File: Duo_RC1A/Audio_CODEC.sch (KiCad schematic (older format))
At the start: 31 parts

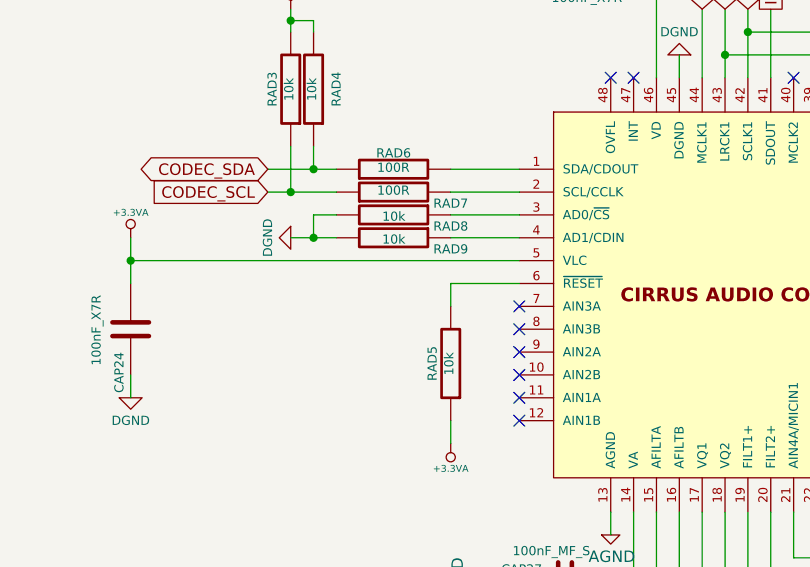
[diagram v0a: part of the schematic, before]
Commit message: Removed some of the audio CODEC signals for Minimal Viable Product. Need to change the 3.3V regulator to the Top Board.
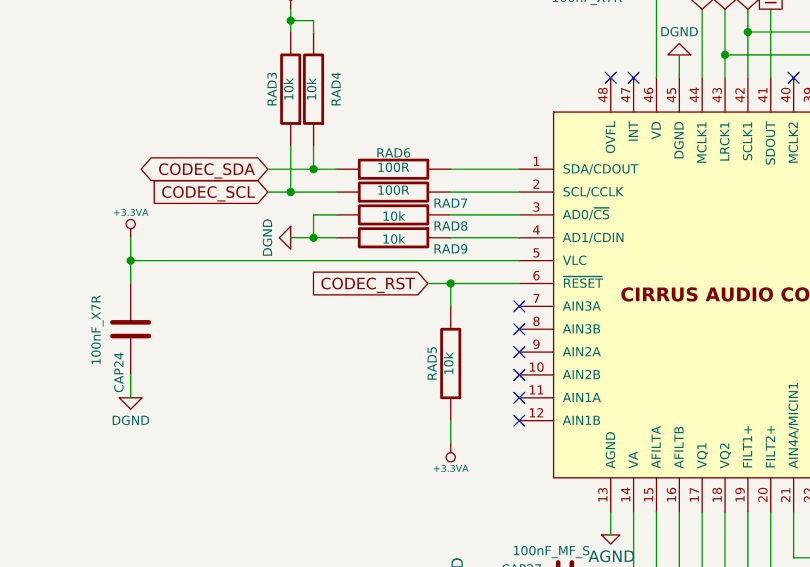
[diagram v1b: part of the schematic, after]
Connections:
- net CODEC_RST: now reaches RAD5.2, UA9.6 (~RESET)
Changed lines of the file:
@@
 Connection ~ 4000 3000
 Wire Wire Line
-	4700 3400 5000 3400
+	4600 3400 5000 3400
 Wire Wire Line
 	4000 2200 4000 2300
@@
 Wire Wire Line
 	2450 5650 2450 5550
+Text GLabel 4600 3400 0    50   Input ~ 0
+CODEC_RST
+Connection ~ 4700 3400
 $EndSCHEMATC

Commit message: Wrking on the sound. Changed the board size.
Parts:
- removed CAP29: 10uF, Duo_Audio_HMI_RC1A:SM0805, symbol CP1
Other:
- moved on the sheet: CAP24, CAP30
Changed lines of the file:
@@
 L C CAP24
 U 1 1 53695313
-P 3300 3600
-F 0 "CAP24" V 3350 3700 40  0000 L CNN
-F 1 "100nF_X7R" V 3450 3450 40  0000 L CNN
-F 2 "Duo_Audio_HMI_RC1A:SM0603" H 3338 3450 30  0001 C CNN
-F 3 "~" H 3300 3600 60  0000 C CNN
-	1    3300 3600
+P 3600 3600
+F 0 "CAP24" V 3650 3700 40  0000 L CNN
+F 1 "100nF_X7R" V 3750 3450 40  0000 L CNN
+F 2 "Duo_Audio_HMI_RC1A:SM0603" H 3638 3450 30  0001 C CNN
+F 3 "~" H 3600 3600 60  0000 C CNN
+	1    3600 3600
 	-1   0    0    1
 $EndComp
@@
 	4700 4000 4700 4100
 Wire Wire Line
-	3300 3200 3300 3400
+	3600 3200 3600 3400
 $Comp
 L +3.3VA #PWR0181
 U 1 1 53696D8F
-P 3300 3200
-F 0 "#PWR0181" H 3300 3160 30  0001 C CNN
-F 1 "+3.3VA" H 3300 3310 30  0000 C CNN
-F 2 "~" H 3300 3200 60  0000 C CNN
-F 3 "~" H 3300 3200 60  0000 C CNN
-	1    3300 3200
-	1    0    0    -1
-$EndComp
-$Comp
-L CP1 CAP29
-U 1 1 53697CB5
-P 5300 1800
-F 0 "CAP29" V 5250 1550 40  0000 L CNN
-F 1 "10uF" V 5440 1720 40  0000 L CNN
-F 2 "Duo_Audio_HMI_RC1A:SM0805" H 5300 1800 60  0001 C CNN
-F 3 "~" H 5300 1800 60  0000 C CNN
-	1    5300 1800
-	0    1    -1   0
+P 3600 3200
+F 0 "#PWR0181" H 3600 3160 30  0001 C CNN
+F 1 "+3.3VA" H 3600 3310 30  0000 C CNN
+F 2 "~" H 3600 3200 60  0000 C CNN
+F 3 "~" H 3600 3200 60  0000 C CNN
+	1    3600 3200
+	1    0    0    -1
 $EndComp
 $Comp
 L C CAP30
 U 1 1 53697CBB
-P 5300 2000
-F 0 "CAP30" V 5350 2100 40  0000 L CNN
-F 1 "100nF_X7R" V 5450 1850 40  0000 L CNN
-F 2 "Duo_Audio_HMI_RC1A:SM0603" H 5338 1850 30  0001 C CNN
-F 3 "~" H 5300 2000 60  0000 C CNN
-	1    5300 2000
+P 5300 2200
+F 0 "CAP30" V 5150 2100 40  0000 L CNN
+F 1 "100nF_X7R" V 5450 2050 40  0000 L CNN
+F 2 "Duo_Audio_HMI_RC1A:SM0603" H 5338 2050 30  0001 C CNN
+F 3 "~" H 5300 2200 60  0000 C CNN
+	1    5300 2200
 	0    -1   1    0
 $EndComp
 Wire Wire Line
-	4900 2000 5100 2000
-Wire Wire Line
-	5000 2000 5000 1800
-Wire Wire Line
-	5000 1800 5100 1800
-Connection ~ 5000 2000
+	5000 2200 5100 2200
 $Comp
 L +3.3VA #PWR0182
 U 1 1 53697CCF
-P 5600 1700
-F 0 "#PWR0182" H 5600 1660 30  0001 C CNN
-F 1 "+3.3VA" H 5600 1810 30  0000 C CNN
-F 2 "~" H 5600 1700 60  0000 C CNN
-F 3 "~" H 5600 1700 60  0000 C CNN
-	1    5600 1700
-	1    0    0    -1
-$EndComp
-Wire Wire Line
-	5600 1700 5600 2500
-Wire Wire Line
-	5600 1800 5500 1800
-Wire Wire Line
-	5500 2000 5600 2000
-Connection ~ 5600 2000
-Connection ~ 5600 1800
+P 5600 2100
+F 0 "#PWR0182" H 5600 2060 30  0001 C CNN
+F 1 "+3.3VA" H 5600 2210 30  0000 C CNN
+F 2 "~" H 5600 2100 60  0000 C CNN
+F 3 "~" H 5600 2100 60  0000 C CNN
+	1    5600 2100
+	1    0    0    -1
+$EndComp
+Wire Wire Line
+	5600 2100 5600 2500
+Wire Wire Line
+	5500 2200 5600 2200
+Connection ~ 5600 2200
 $Comp
 L DGND #PWR0183
 U 1 1 53698221
-P 4900 2000
-F 0 "#PWR0183" H 4900 2000 40  0001 C CNN
-F 1 "DGND" H 4900 1900 40  0000 C CNN
-F 2 "~" H 4900 2000 60  0000 C CNN
-F 3 "~" H 4900 2000 60  0000 C CNN
-	1    4900 2000
+P 5000 2200
+F 0 "#PWR0183" H 5000 2200 40  0001 C CNN
+F 1 "DGND" H 5000 2100 40  0000 C CNN
+F 2 "~" H 5000 2200 60  0000 C CNN
+F 3 "~" H 5000 2200 60  0000 C CNN
+	1    5000 2200
 	0    1    1    0
 $EndComp
@@
 L DGND #PWR0185
 U 1 1 5369C1E0
-P 3300 3900
-F 0 "#PWR0185" H 3300 3900 40  0001 C CNN
-F 1 "DGND" H 3300 3800 40  0000 C CNN
-F 2 "~" H 3300 3900 60  0000 C CNN
-F 3 "~" H 3300 3900 60  0000 C CNN
-	1    3300 3900
+P 3600 3900
+F 0 "#PWR0185" H 3600 3900 40  0001 C CNN
+F 1 "DGND" H 3600 3800 40  0000 C CNN
+F 2 "~" H 3600 3900 60  0000 C CNN
+F 3 "~" H 3600 3900 60  0000 C CNN
+	1    3600 3900
 	1    0    0    -1
 $EndComp
@@
 NoConn ~ 5000 3500
 Wire Wire Line
-	3300 3900 3300 3800
-Wire Wire Line
-	5000 3300 3300 3300
-Connection ~ 3300 3300
+	3600 3900 3600 3800
+Wire Wire Line
+	5000 3300 3600 3300
+Connection ~ 3600 3300
 Wire Wire Line
 	5800 2200 5800 2500

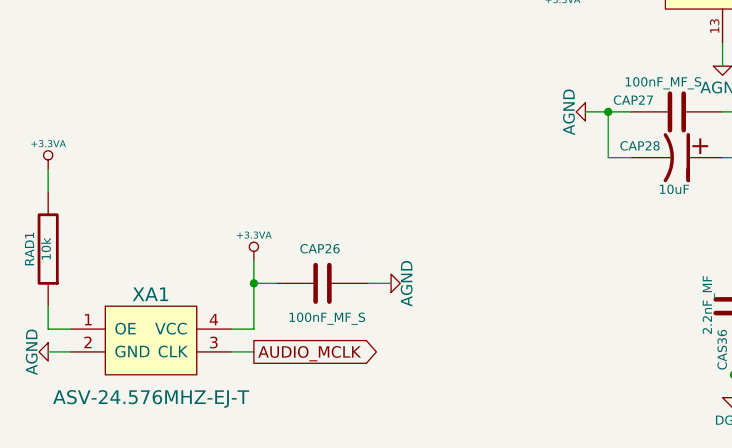
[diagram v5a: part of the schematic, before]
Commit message: USB OTG and HOST traks done.
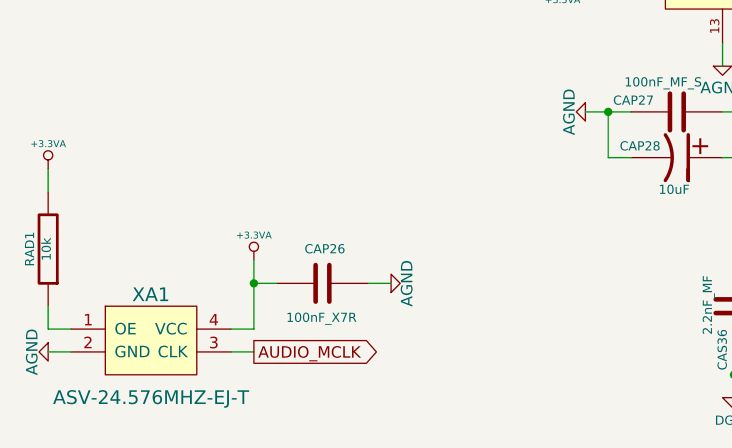
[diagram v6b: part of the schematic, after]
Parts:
- CAP26: value 100nF_MF_S -> 100nF_X7R; footprint Duo_Audio_HMI_RC1A:CapacitorMetalFilm_7.2x2.5MM_P5MM -> Duo_Audio_HMI_RC1A:SM0603
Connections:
- net +3.3VA: now also CAP26.1; no longer CAP26.2
- net AGND: now also CAP26.2; no longer CAP26.1
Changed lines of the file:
@@
 $EndComp
 $Comp
-L AGND #PWR0182
+L AGND #PWR0186
 U 1 1 5369103E
 P 2450 5750
-F 0 "#PWR0182" H 2450 5750 40  0001 C CNN
+F 0 "#PWR0186" H 2450 5750 40  0001 C CNN
 F 1 "AGND" H 2450 5680 50  0000 C CNN
 F 2 "~" H 2450 5750 60  0000 C CNN
@@
 $EndComp
 $Comp
-L +3.3VA #PWR0183
+L +3.3VA #PWR0187
 U 1 1 53691514
 P 3350 5350
-F 0 "#PWR0183" H 3350 5310 30  0001 C CNN
+F 0 "#PWR0187" H 3350 5310 30  0001 C CNN
 F 1 "+3.3VA" H 3350 5460 30  0000 C CNN
 F 2 "~" H 3350 5350 60  0000 C CNN
@@
 $EndComp
 $Comp
-L C CAP26
-U 1 1 5369152B
-P 3650 5450
-F 0 "CAP26" V 3500 5350 40  0000 L CNN
-F 1 "100nF_MF_S" V 3800 5300 40  0000 L CNN
-F 2 "Duo_Audio_HMI_RC1A:CapacitorMetalFilm_7.2x2.5MM_P5MM" H 3688 5300 30  0001 C CNN
-F 3 "~" H 3650 5450 60  0000 C CNN
-	1    3650 5450
-	0    1    1    0
-$EndComp
-$Comp
-L AGND #PWR0184
+L AGND #PWR0188
 U 1 1 53691576
 P 3950 5450
-F 0 "#PWR0184" H 3950 5450 40  0001 C CNN
+F 0 "#PWR0188" H 3950 5450 40  0001 C CNN
 F 1 "AGND" H 3950 5380 50  0000 C CNN
 F 2 "~" H 3950 5450 60  0000 C CNN
@@
 $EndComp
 $Comp
-L +3.3VA #PWR0185
+L +3.3VA #PWR0189
 U 1 1 536967F3
 P 4000 2200
-F 0 "#PWR0185" H 4000 2160 30  0001 C CNN
+F 0 "#PWR0189" H 4000 2160 30  0001 C CNN
 F 1 "+3.3VA" H 4000 2310 30  0000 C CNN
 F 2 "~" H 4000 2200 60  0000 C CNN
@@
 	3600 3200 3600 3400
 $Comp
-L +3.3VA #PWR0186
+L +3.3VA #PWR0190
 U 1 1 53696D8F
 P 3600 3200
-F 0 "#PWR0186" H 3600 3160 30  0001 C CNN
+F 0 "#PWR0190" H 3600 3160 30  0001 C CNN
 F 1 "+3.3VA" H 3600 3310 30  0000 C CNN
 F 2 "~" H 3600 3200 60  0000 C CNN
@@
 	5000 2200 5100 2200
 $Comp
-L +3.3VA #PWR0187
+L +3.3VA #PWR0191
 U 1 1 53697CCF
 P 5600 2100
-F 0 "#PWR0187" H 5600 2060 30  0001 C CNN
+F 0 "#PWR0191" H 5600 2060 30  0001 C CNN
 F 1 "+3.3VA" H 5600 2210 30  0000 C CNN
 F 2 "~" H 5600 2100 60  0000 C CNN
@@
 Connection ~ 5600 2200
 $Comp
-L DGND #PWR0188
+L DGND #PWR0192
 U 1 1 53698221
 P 5000 2200
-F 0 "#PWR0188" H 5000 2200 40  0001 C CNN
+F 0 "#PWR0192" H 5000 2200 40  0001 C CNN
 F 1 "DGND" H 5000 2100 40  0000 C CNN
 F 2 "~" H 5000 2200 60  0000 C CNN
@@
 $EndComp
 $Comp
-L DGND #PWR0189
+L DGND #PWR0193
 U 1 1 53698262
 P 5700 2400
-F 0 "#PWR0189" H 5700 2400 40  0001 C CNN
+F 0 "#PWR0193" H 5700 2400 40  0001 C CNN
 F 1 "DGND" H 5700 2300 40  0000 C CNN
 F 2 "~" H 5700 2400 60  0000 C CNN
@@
 Connection ~ 5900 2400
 $Comp
-L DGND #PWR0190
+L DGND #PWR0194
 U 1 1 5369C1E0
 P 3600 3900
-F 0 "#PWR0190" H 3600 3900 40  0001 C CNN
+F 0 "#PWR0194" H 3600 3900 40  0001 C CNN
 F 1 "DGND" H 3600 3800 40  0000 C CNN
 F 2 "~" H 3600 3900 60  0000 C CNN
@@
 $EndComp
 $Comp
-L AGND #PWR0191
+L AGND #PWR0195
 U 1 1 5369C69C
 P 5400 4500
-F 0 "#PWR0191" H 5400 4500 40  0001 C CNN
+F 0 "#PWR0195" H 5400 4500 40  0001 C CNN
 F 1 "AGND" H 5405 4405 50  0000 C CNN
 F 2 "~" H 5400 4500 60  0000 C CNN
@@
 	5400 4400 5400 4500
 $Comp
-L AGND #PWR0192
+L AGND #PWR0196
 U 1 1 5369C6F4
 P 7000 3400
-F 0 "#PWR0192" H 7000 3400 40  0001 C CNN
+F 0 "#PWR0196" H 7000 3400 40  0001 C CNN
 F 1 "AGND" H 7000 3330 50  0000 C CNN
 F 2 "~" H 7000 3400 60  0000 C CNN
@@
 	7500 2700 7600 2700
 $Comp
-L +3.3VA #PWR0193
+L +3.3VA #PWR0197
 U 1 1 5369D63F
 P 7000 2600
-F 0 "#PWR0193" H 7000 2560 30  0001 C CNN
+F 0 "#PWR0197" H 7000 2560 30  0001 C CNN
 F 1 "+3.3VA" H 7000 2710 30  0000 C CNN
 F 2 "~" H 7000 2600 60  0000 C CNN
@@
 Connection ~ 7000 2700
 $Comp
-L DGND #PWR0194
+L DGND #PWR0198
 U 1 1 5369D64A
 P 7600 2700
-F 0 "#PWR0194" H 7600 2700 40  0001 C CNN
+F 0 "#PWR0198" H 7600 2700 40  0001 C CNN
 F 1 "DGND" H 7600 2600 40  0000 C CNN
 F 2 "~" H 7600 2700 60  0000 C CNN
@@
 Connection ~ 5500 4900
 $Comp
-L +5VA #PWR0195
+L +5VA #PWR0199
 U 1 1 5369E57F
 P 5500 5000
-F 0 "#PWR0195" H 5500 5130 20  0001 C CNN
+F 0 "#PWR0199" H 5500 5130 20  0001 C CNN
 F 1 "+5VA" H 5500 5100 30  0000 C CNN
 F 2 "~" H 5500 5000 60  0000 C CNN
@@
 Connection ~ 6150 5850
 $Comp
-L DGND #PWR0196
+L DGND #PWR0200
 U 1 1 536A0C40
 P 6150 5950
-F 0 "#PWR0196" H 6150 5950 40  0001 C CNN
+F 0 "#PWR0200" H 6150 5950 40  0001 C CNN
 F 1 "DGND" H 6150 5850 40  0000 C CNN
 F 2 "~" H 6150 5950 60  0000 C CNN
@@
 $EndComp
 $Comp
-L AGND #PWR0197
+L AGND #PWR0201
 U 1 1 536A0C51
 P 4800 4700
-F 0 "#PWR0197" H 4800 4700 40  0001 C CNN
+F 0 "#PWR0201" H 4800 4700 40  0001 C CNN
 F 1 "AGND" H 4800 4630 50  0000 C CNN
 F 2 "~" H 4800 4700 60  0000 C CNN
@@
 $EndComp
 $Comp
-L DGND #PWR0198
+L DGND #PWR0202
 U 1 1 536A11E5
 P 5450 5950
-F 0 "#PWR0198" H 5450 5950 40  0001 C CNN
+F 0 "#PWR0202" H 5450 5950 40  0001 C CNN
 F 1 "DGND" H 5450 5850 40  0000 C CNN
 F 2 "~" H 5450 5950 60  0000 C CNN
@@
 Connection ~ 6700 5850
 $Comp
-L DGND #PWR0199
+L DGND #PWR0203
 U 1 1 536A12DC
 P 6700 5950
-F 0 "#PWR0199" H 6700 5950 40  0001 C CNN
+F 0 "#PWR0203" H 6700 5950 40  0001 C CNN
 F 1 "DGND" H 6700 5850 40  0000 C CNN
 F 2 "~" H 6700 5950 60  0000 C CNN
@@
 Connection ~ 7250 5850
 $Comp
-L DGND #PWR0200
+L DGND #PWR0204
 U 1 1 536A12F3
 P 7250 5950
-F 0 "#PWR0200" H 7250 5950 40  0001 C CNN
+F 0 "#PWR0204" H 7250 5950 40  0001 C CNN
 F 1 "DGND" H 7250 5850 40  0000 C CNN
 F 2 "~" H 7250 5950 60  0000 C CNN
@@
 Connection ~ 7800 5850
 $Comp
-L DGND #PWR0201
+L DGND #PWR0205
 U 1 1 536A130A
 P 7800 5950
-F 0 "#PWR0201" H 7800 5950 40  0001 C CNN
+F 0 "#PWR0205" H 7800 5950 40  0001 C CNN
 F 1 "DGND" H 7800 5850 40  0000 C CNN
 F 2 "~" H 7800 5950 60  0000 C CNN
@@
 Connection ~ 7200 3500
 $Comp
-L +5VA #PWR0202
+L +5VA #PWR0206
 U 1 1 536A2B75
 P 7400 3400
-F 0 "#PWR0202" H 7400 3530 20  0001 C CNN
+F 0 "#PWR0206" H 7400 3530 20  0001 C CNN
 F 1 "+5VA" H 7400 3500 30  0000 C CNN
 F 2 "~" H 7400 3400 60  0000 C CNN
@@
 $EndComp
 $Comp
-L AGND #PWR0203
+L AGND #PWR0207
 U 1 1 536A2B7C
 P 7400 4200
-F 0 "#PWR0203" H 7400 4200 40  0001 C CNN
+F 0 "#PWR0207" H 7400 4200 40  0001 C CNN
 F 1 "AGND" H 7400 4130 50  0000 C CNN
 F 2 "~" H 7400 4200 60  0000 C CNN
@@
 Connection ~ 8450 4600
 $Comp
-L AGND #PWR0204
+L AGND #PWR0208
 U 1 1 536A45D9
 P 7950 4200
-F 0 "#PWR0204" H 7950 4200 40  0001 C CNN
+F 0 "#PWR0208" H 7950 4200 40  0001 C CNN
 F 1 "AGND" H 7950 4130 50  0000 C CNN
 F 2 "~" H 7950 4200 60  0000 C CNN
@@
 	7950 4200 8050 4200
 $Comp
-L AGND #PWR0205
+L AGND #PWR0209
 U 1 1 536A467E
 P 7950 4900
-F 0 "#PWR0205" H 7950 4900 40  0001 C CNN
+F 0 "#PWR0209" H 7950 4900 40  0001 C CNN
 F 1 "AGND" H 7950 4830 50  0000 C CNN
 F 2 "~" H 7950 4900 60  0000 C CNN
@@
 	7950 4900 8050 4900
 $Comp
-L +5VA #PWR0206
+L +5VA #PWR0210
 U 1 1 536A4685
 P 8950 4900
-F 0 "#PWR0206" H 8950 5030 20  0001 C CNN
+F 0 "#PWR0210" H 8950 5030 20  0001 C CNN
 F 1 "+5VA" H 8950 5000 30  0000 C CNN
 F 2 "~" H 8950 4900 60  0000 C CNN
@@
 	8850 4900 8950 4900
 $Comp
-L +5VA #PWR0207
+L +5VA #PWR0211
 U 1 1 536A472C
 P 8950 4200
-F 0 "#PWR0207" H 8950 4330 20  0001 C CNN
+F 0 "#PWR0211" H 8950 4330 20  0001 C CNN
 F 1 "+5VA" H 8950 4300 30  0000 C CNN
 F 2 "~" H 8950 4200 60  0000 C CNN
@@
 	4000 3200 4200 3200
 $Comp
-L DGND #PWR0208
+L DGND #PWR0212
 U 1 1 536BE92A
 P 4000 3200
-F 0 "#PWR0208" H 4000 3200 40  0001 C CNN
+F 0 "#PWR0212" H 4000 3200 40  0001 C CNN
 F 1 "DGND" H 4000 3100 40  0000 C CNN
 F 2 "~" H 4000 3200 60  0000 C CNN
@@
 NoConn ~ 5500 2500
 $Comp
-L +3.3VA #PWR0209
+L +3.3VA #PWR0213
 U 1 1 538CDEC8
 P 4700 4100
-F 0 "#PWR0209" H 4700 4060 30  0001 C CNN
+F 0 "#PWR0213" H 4700 4060 30  0001 C CNN
 F 1 "+3.3VA" H 4700 4210 30  0000 C CNN
 F 2 "~" H 4700 4100 60  0000 C CNN
@@
 	4700 3400 4700 3500
 $Comp
-L +3.3VA #PWR0210
+L +3.3VA #PWR0214
 U 1 1 538CECDF
 P 2450 4950
-F 0 "#PWR0210" H 2450 4910 30  0001 C CNN
+F 0 "#PWR0214" H 2450 4910 30  0001 C CNN
 F 1 "+3.3VA" H 2450 5060 30  0000 C CNN
 F 2 "~" H 2450 4950 60  0000 C CNN
@@
 CODEC_RST
 Connection ~ 4700 3400
+$Comp
+L C CAP26
+U 1 1 53D0745F
+P 3650 5450
+F 0 "CAP26" V 3800 5350 40  0000 L CNN
+F 1 "100nF_X7R" V 3500 5300 40  0000 L CNN
+F 2 "Duo_Audio_HMI_RC1A:SM0603" H 3688 5300 30  0001 C CNN
+F 3 "~" H 3650 5450 60  0000 C CNN
+	1    3650 5450
+	0    -1   -1   0
+$EndComp
 $EndSCHEMATC

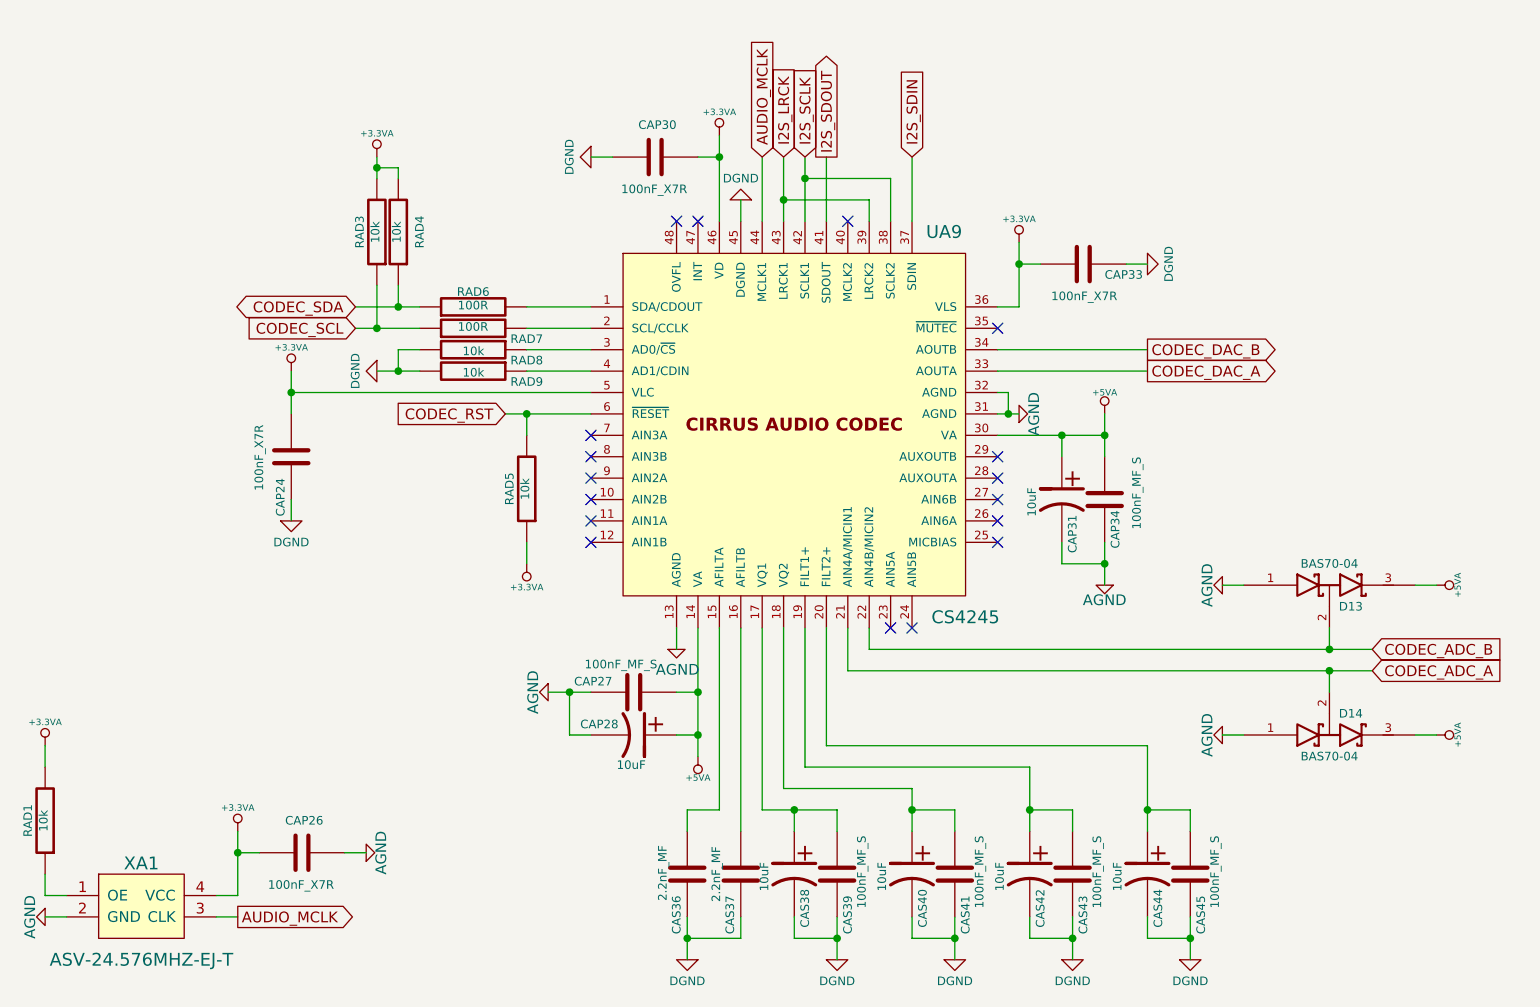
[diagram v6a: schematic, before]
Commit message: Working on the soundcard tracks.
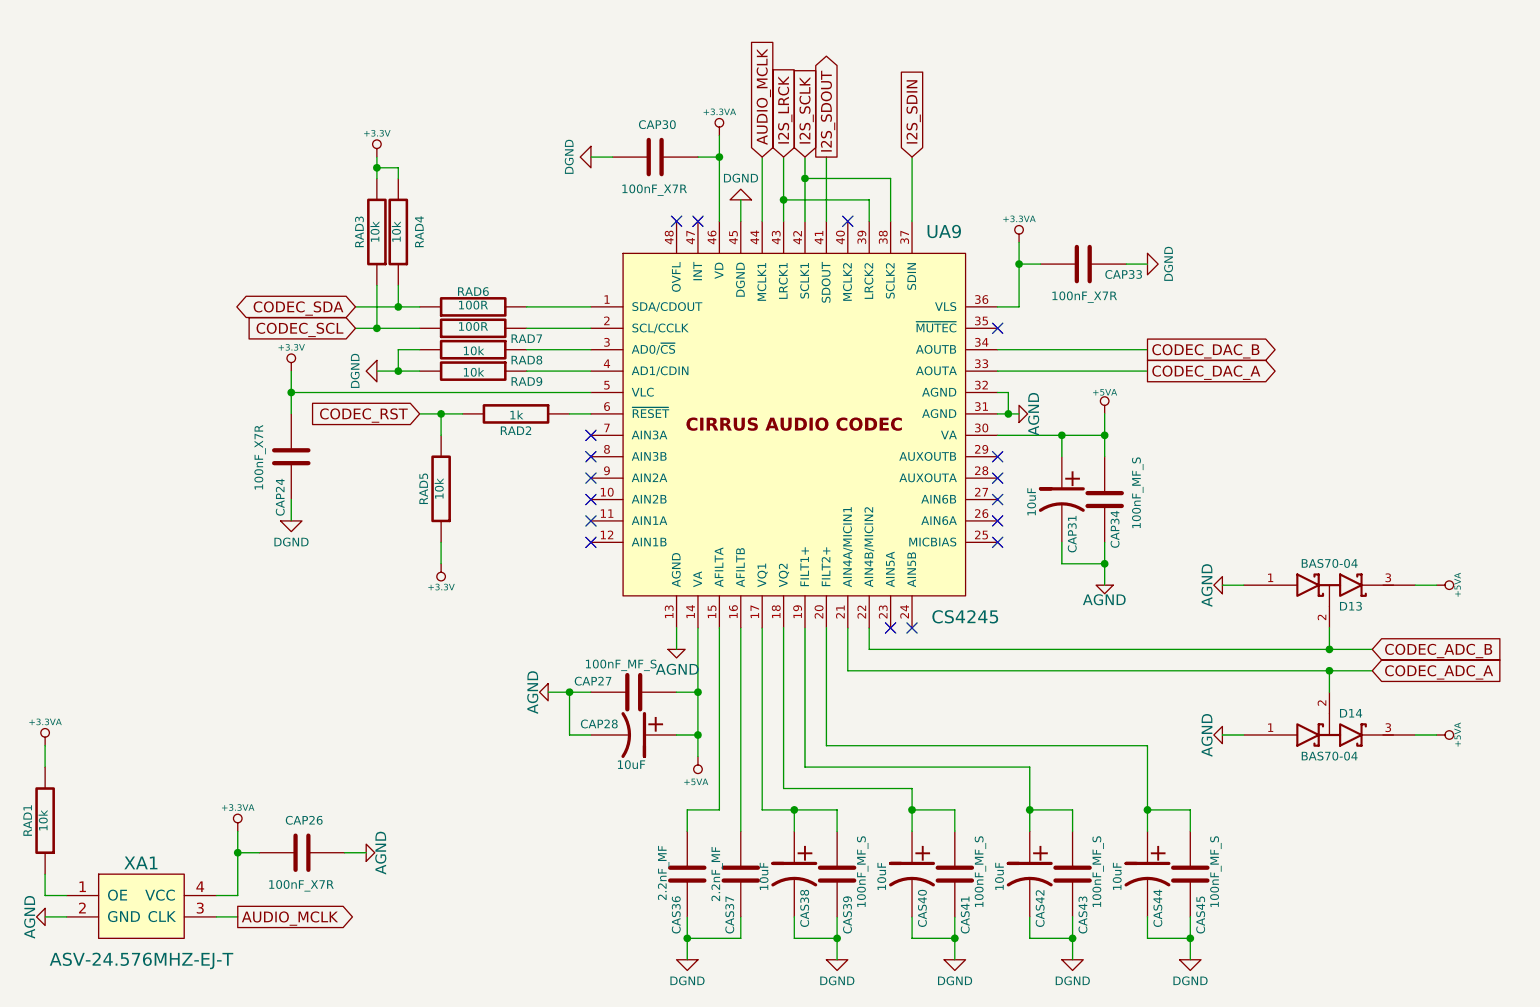
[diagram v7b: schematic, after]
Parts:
- added RAD2: 1k, Duo_Audio_HMI_RC1A:SM0603, symbol R
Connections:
- net +3.3VA: no longer CAP24.2, RAD3.2, RAD4.2, RAD5.1, UA9.5 (VLC)
- net CODEC_RST: now also RAD2.2; no longer UA9.6 (~RESET)
- new net: RAD2.1, UA9.6 (~RESET)
- new net +3.3V: CAP24.2, RAD3.2, RAD4.2, RAD5.1, UA9.5 (VLC)
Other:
- moved on the sheet: RAD5
